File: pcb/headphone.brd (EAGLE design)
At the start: 94 x 35.6 mm, 29 parts, among them IC101 LF353D, IC201 LF353N, IC301 LF353N, J101 MONOJACKSWITCHCRAFT3, J102 MONOJACKSWITCHCRAFT3, J201 MONOJACKNEUTRIK, J202 MONOJACKNEUTRIK, J301 STEREOJACK, J401 POWER_SIMPLE16, P101 DUALPOT 50K

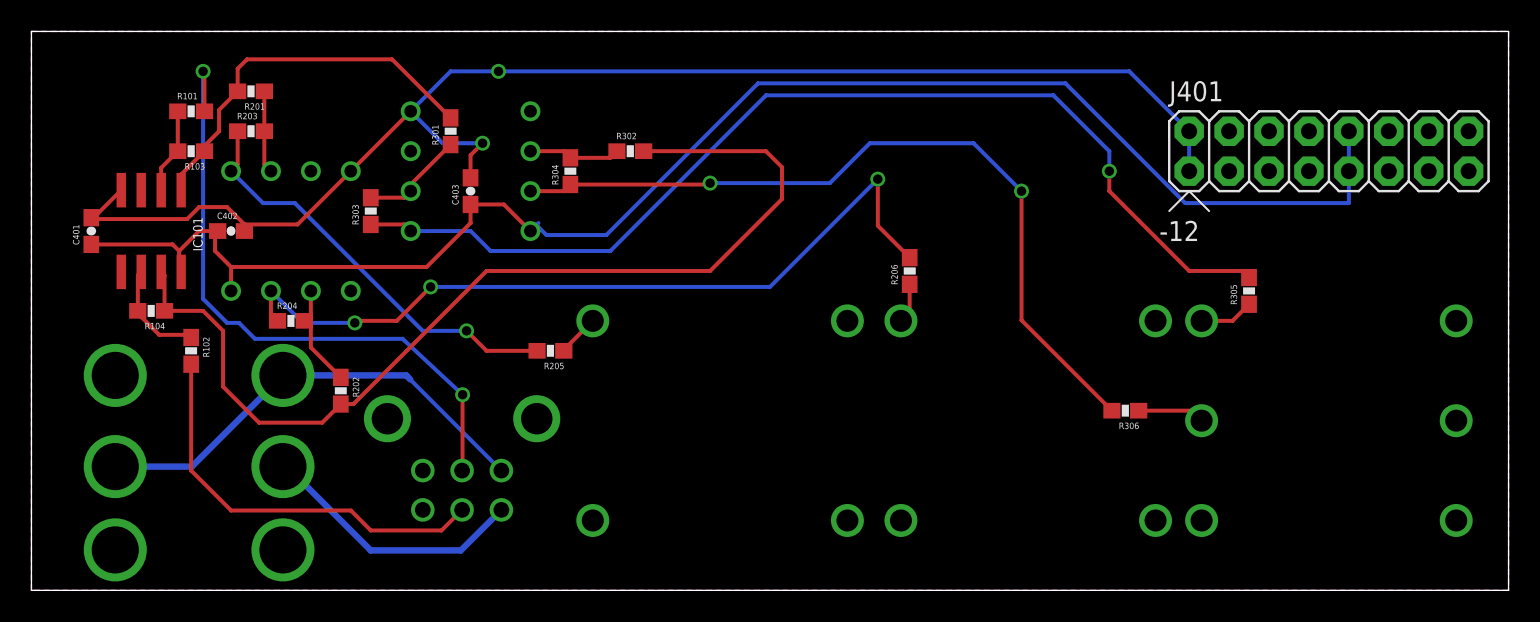
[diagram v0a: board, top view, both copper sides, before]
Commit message: added silkscreen
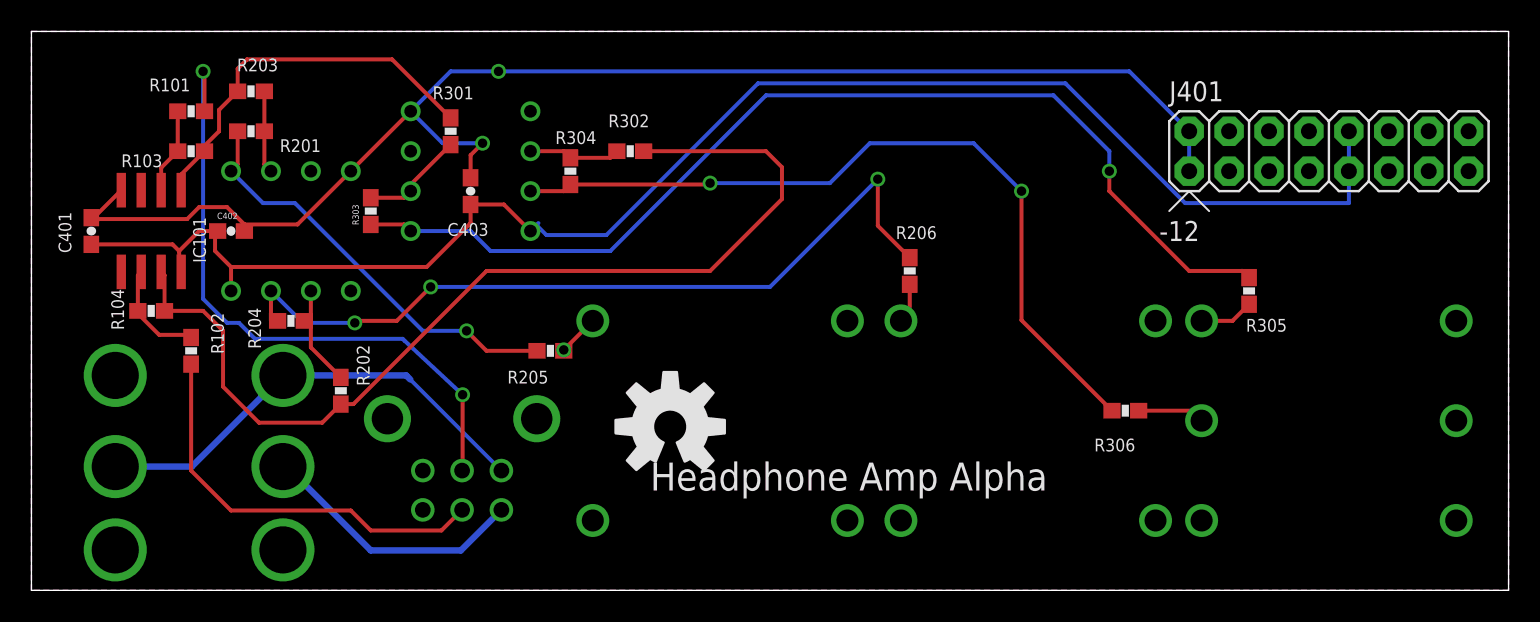
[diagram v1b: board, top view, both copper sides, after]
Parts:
- added U$1: (no value), SparkFun:OSHW-LOGO-L
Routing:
- net N$12: vias 0 -> 1
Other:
- board text added: "Headphone Amp Alpha"
